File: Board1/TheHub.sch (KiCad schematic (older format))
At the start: 27 parts

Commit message: Add support for RFD900 on USART6
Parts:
- added J?: RFD900, symbol CONN_02X08
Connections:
- net GND: now also J?.1 (P1), J?.16 (P16), J?.2 (P2)
- net PA11: now also J?.7 (P7)
- net PA12: now also J?.9 (P9)
- net 5V renamed +5V
- net +5V: now also J?.4 (P4)
- no-connect marks 19 -> 29
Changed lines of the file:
@@
 NoConn ~ 7650 6750
 NoConn ~ 11150 6750
+$Comp
+L CONN_02X08 J?
+U 1 1 59371070
+P 13700 2900
+F 0 "J?" H 13700 3350 50  0000 C CNN
+F 1 "RFD900" V 13700 2900 50  0000 C CNN
+F 2 "" H 13700 1700 50  0001 C CNN
+F 3 "" H 13700 1700 50  0001 C CNN
+	1    13700 2900
+	1    0    0    -1
+$EndComp
+Text Label 13450 2550 2    60   ~ 0
+GND
+NoConn ~ 13450 2650
+NoConn ~ 13450 2750
+NoConn ~ 13450 3050
+NoConn ~ 13450 3150
+NoConn ~ 13450 3250
+NoConn ~ 13950 3150
+NoConn ~ 13950 3050
+NoConn ~ 13950 2950
+NoConn ~ 13950 2850
+NoConn ~ 13950 2750
+Text Label 13950 2550 0    60   ~ 0
+GND
+Text Label 13950 2650 0    60   ~ 0
+5V
+$Comp
+L +5V #PWR?
+U 1 1 593718A3
+P 14250 2650
+F 0 "#PWR?" H 14250 2500 50  0001 C CNN
+F 1 "+5V" H 14250 2790 50  0000 C CNN
+F 2 "" H 14250 2650 50  0001 C CNN
+F 3 "" H 14250 2650 50  0001 C CNN
+	1    14250 2650
+	1    0    0    -1
+$EndComp
+Wire Wire Line
+	14250 2650 13950 2650
+Wire Wire Line
+	13950 2550 13950 2350
+Wire Wire Line
+	13950 2350 13450 2350
+Wire Wire Line
+	13450 2350 13450 2550
+$Comp
+L GND #PWR?
+U 1 1 59371A35
+P 13750 2350
+F 0 "#PWR?" H 13750 2100 50  0001 C CNN
+F 1 "GND" H 13750 2200 50  0000 C CNN
+F 2 "" H 13750 2350 50  0001 C CNN
+F 3 "" H 13750 2350 50  0001 C CNN
+	1    13750 2350
+	-1   0    0    1
+$EndComp
+Wire Wire Line
+	5450 2550 6050 2550
+Wire Wire Line
+	5450 2450 6050 2450
+Text Label 6050 2550 0    60   ~ 0
+USART6_TX
+Text Label 6050 2450 0    60   ~ 0
+USART6_RX
+Text Label 13450 2850 2    60   ~ 0
+USART6_TX
+Text Label 13450 2950 2    60   ~ 0
+USART6_RX
+$Comp
+L GND #PWR?
+U 1 1 59372AF7
+P 14150 3250
+F 0 "#PWR?" H 14150 3000 50  0001 C CNN
+F 1 "GND" H 14150 3100 50  0000 C CNN
+F 2 "" H 14150 3250 50  0001 C CNN
+F 3 "" H 14150 3250 50  0001 C CNN
+	1    14150 3250
+	0    -1   -1   0
+$EndComp
+Wire Wire Line
+	14150 3250 13950 3250
 $EndSCHEMATC

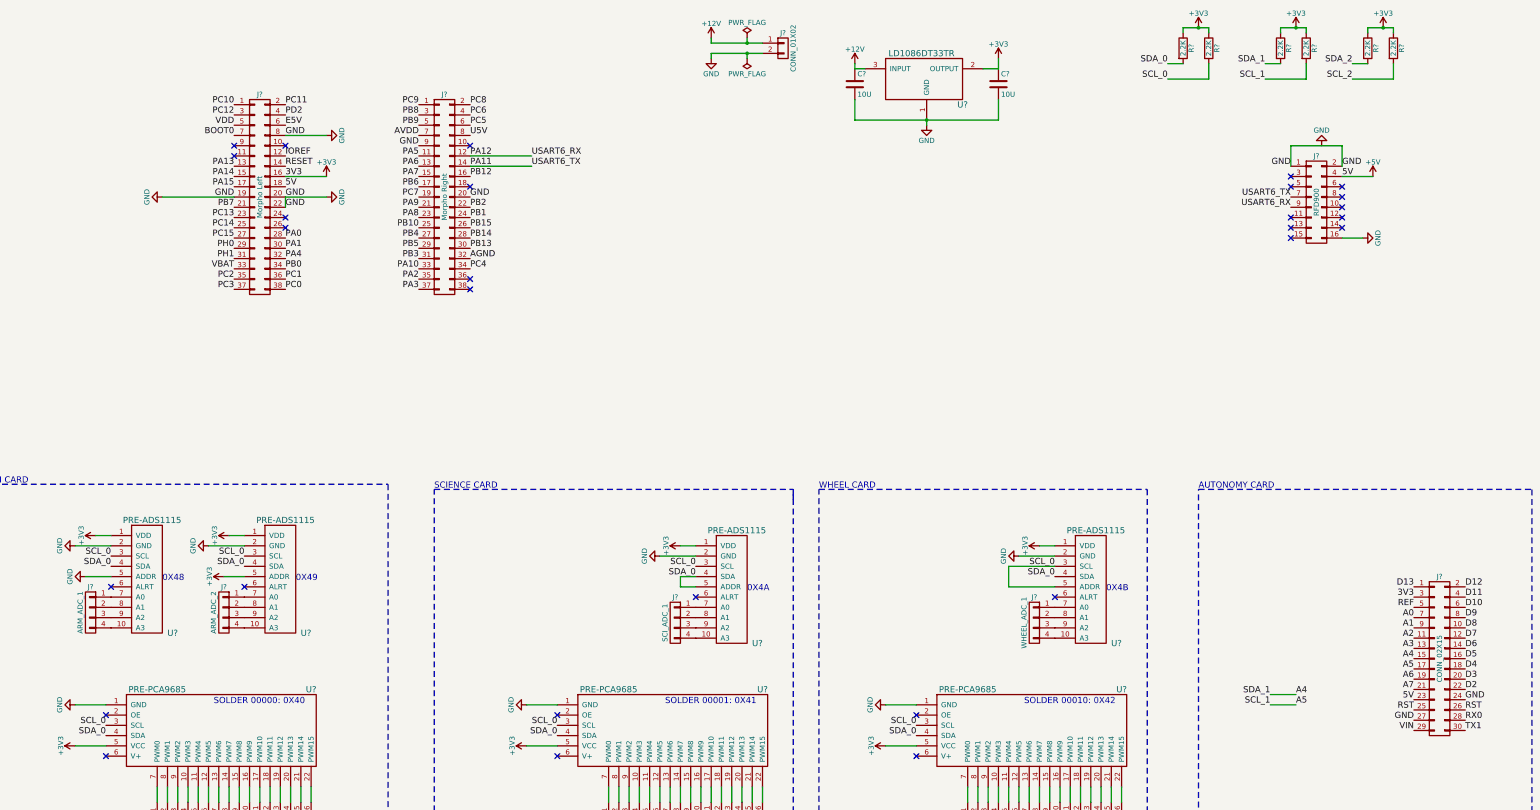
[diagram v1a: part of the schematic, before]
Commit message: Change I2C lines to properly index
I2C starts at 1, not 0
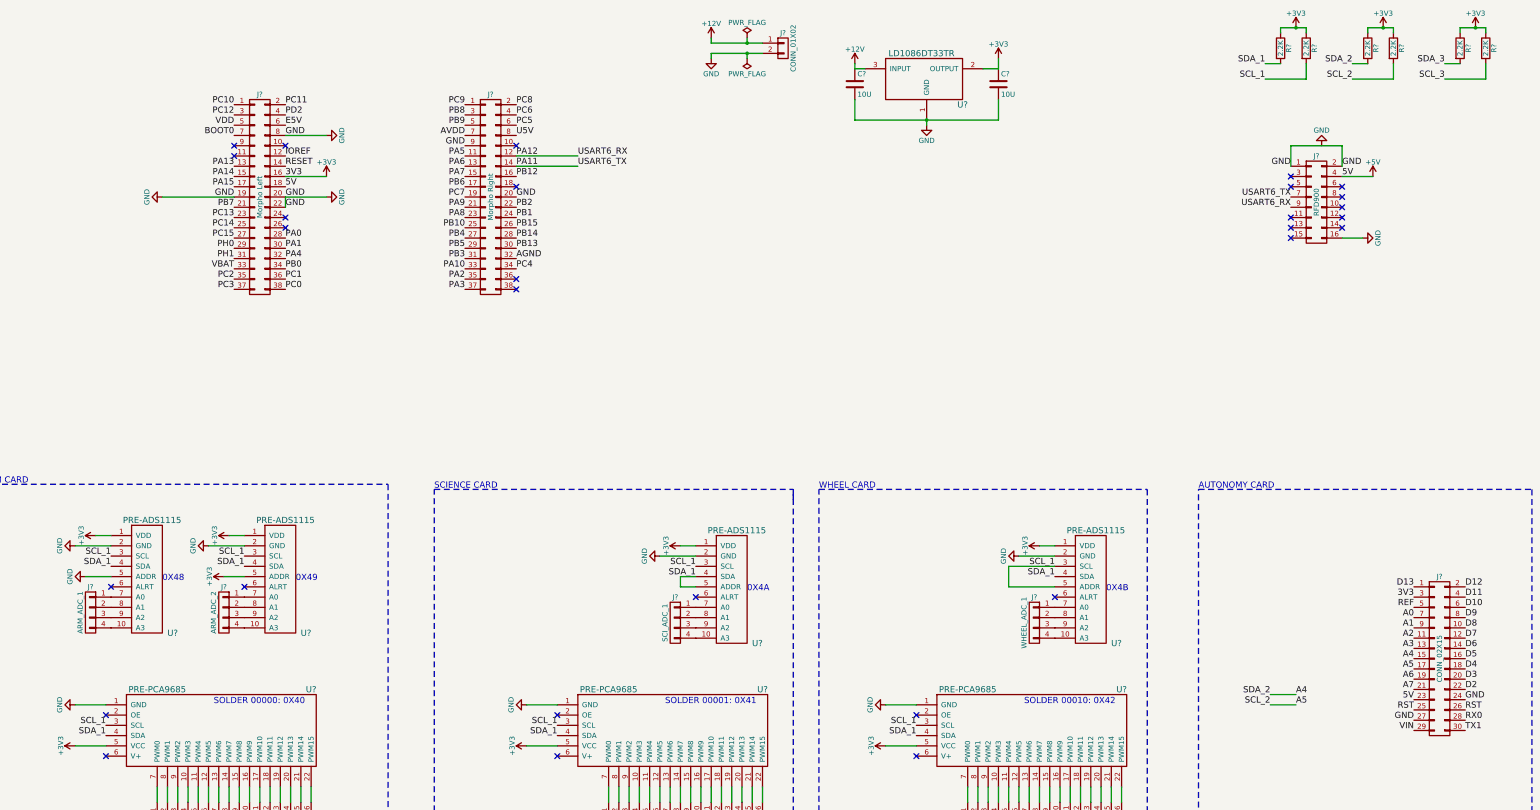
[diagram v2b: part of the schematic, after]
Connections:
- net SCL_2 is gone; now on net A5: R?.2
- net SDA_2 is gone; now on net A4: R?.2
- net A4: no longer R?.2
- net A5: no longer R?.2
- net SCL_0 renamed SCL_1
- net SCL_1: now also R?.2; no longer R?.2
- net SDA_0 renamed SDA_1
- net SDA_1: now also R?.2; no longer R?.2
- new net SCL_3: R?.2
- new net SDA_3: R?.2
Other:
- moved on the sheet: J?, R?
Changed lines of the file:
@@
 L CONN_02X19 J?
 U 1 1 5935F6CD
-P 5200 2850
-F 0 "J?" H 5200 3850 50  0000 C CNN
-F 1 "Morpho Right" V 5200 2850 50  0000 C CNN
-F 2 "" H 5200 1850 50  0001 C CNN
-F 3 "" H 5200 1850 50  0001 C CNN
-	1    5200 2850
+P 5650 2850
+F 0 "J?" H 5650 3850 50  0000 C CNN
+F 1 "Morpho Right" V 5650 2850 50  0000 C CNN
+F 2 "" H 5650 1850 50  0001 C CNN
+F 3 "" H 5650 1850 50  0001 C CNN
+	1    5650 2850
 	1    0    0    -1
 $EndComp
@@
 Text Label 3650 3750 0    60   ~ 0
 PC0
-Text Label 4950 1950 2    60   ~ 0
+Text Label 5400 1950 2    60   ~ 0
 PC9
-Text Label 4950 2050 2    60   ~ 0
+Text Label 5400 2050 2    60   ~ 0
 PB8
-Text Label 4950 2150 2    60   ~ 0
+Text Label 5400 2150 2    60   ~ 0
 PB9
-Text Label 4950 2250 2    60   ~ 0
+Text Label 5400 2250 2    60   ~ 0
 AVDD
-Text Label 4950 2350 2    60   ~ 0
+Text Label 5400 2350 2    60   ~ 0
 GND
-Text Label 4950 2450 2    60   ~ 0
+Text Label 5400 2450 2    60   ~ 0
 PA5
-Text Label 4950 2550 2    60   ~ 0
+Text Label 5400 2550 2    60   ~ 0
 PA6
-Text Label 4950 2650 2    60   ~ 0
+Text Label 5400 2650 2    60   ~ 0
 PA7
-Text Label 4950 2750 2    60   ~ 0
+Text Label 5400 2750 2    60   ~ 0
 PB6
-Text Label 4950 2850 2    60   ~ 0
+Text Label 5400 2850 2    60   ~ 0
 PC7
-Text Label 4950 2950 2    60   ~ 0
+Text Label 5400 2950 2    60   ~ 0
 PA9
-Text Label 4950 3050 2    60   ~ 0
+Text Label 5400 3050 2    60   ~ 0
 PA8
-Text Label 4950 3150 2    60   ~ 0
+Text Label 5400 3150 2    60   ~ 0
 PB10
-Text Label 4950 3250 2    60   ~ 0
+Text Label 5400 3250 2    60   ~ 0
 PB4
-Text Label 4950 3350 2    60   ~ 0
+Text Label 5400 3350 2    60   ~ 0
 PB5
-Text Label 4950 3450 2    60   ~ 0
+Text Label 5400 3450 2    60   ~ 0
 PB3
-Text Label 4950 3550 2    60   ~ 0
+Text Label 5400 3550 2    60   ~ 0
 PA10
-Text Label 4950 3650 2    60   ~ 0
+Text Label 5400 3650 2    60   ~ 0
 PA2
-Text Label 4950 3750 2    60   ~ 0
+Text Label 5400 3750 2    60   ~ 0
 PA3
-Text Label 5450 1950 0    60   ~ 0
+Text Label 5900 1950 0    60   ~ 0
 PC8
-Text Label 5450 2050 0    60   ~ 0
+Text Label 5900 2050 0    60   ~ 0
 PC6
-Text Label 5450 2150 0    60   ~ 0
+Text Label 5900 2150 0    60   ~ 0
 PC5
-Text Label 5450 2250 0    60   ~ 0
+Text Label 5900 2250 0    60   ~ 0
 U5V
-NoConn ~ 5450 2350
-Text Label 5450 2450 0    60   ~ 0
+NoConn ~ 5900 2350
+Text Label 5900 2450 0    60   ~ 0
 PA12
-Text Label 5450 2550 0    60   ~ 0
+Text Label 5900 2550 0    60   ~ 0
 PA11
-Text Label 5450 2650 0    60   ~ 0
+Text Label 5900 2650 0    60   ~ 0
 PB12
-NoConn ~ 5450 2750
-Text Label 5450 2850 0    60   ~ 0
+NoConn ~ 5900 2750
+Text Label 5900 2850 0    60   ~ 0
 GND
-Text Label 5450 2950 0    60   ~ 0
+Text Label 5900 2950 0    60   ~ 0
 PB2
-Text Label 5450 3050 0    60   ~ 0
+Text Label 5900 3050 0    60   ~ 0
 PB1
-Text Label 5450 3150 0    60   ~ 0
+Text Label 5900 3150 0    60   ~ 0
 PB15
-Text Label 5450 3250 0    60   ~ 0
+Text Label 5900 3250 0    60   ~ 0
 PB14
-Text Label 5450 3350 0    60   ~ 0
+Text Label 5900 3350 0    60   ~ 0
 PB13
-Text Label 5450 3450 0    60   ~ 0
+Text Label 5900 3450 0    60   ~ 0
 AGND
-Text Label 5450 3550 0    60   ~ 0
+Text Label 5900 3550 0    60   ~ 0
 PC4
-NoConn ~ 5450 3650
-NoConn ~ 5450 3750
+NoConn ~ 5900 3650
+NoConn ~ 5900 3750
 Text Label 3650 2650 0    60   ~ 0
 3V3
@@
 TX1
 Text Label 13250 7700 2    60   ~ 0
-SDA_1
+SDA_2
 Text Label 13250 7800 2    60   ~ 0
-SCL_1
+SCL_2
 Text Label 13500 7700 0    60   ~ 0
 A4
 Text Label 13500 7800 0    60   ~ 0
 A5
-Text Label 12250 1550 2    60   ~ 0
-SDA_0
-Text Label 12250 1700 2    60   ~ 0
-SCL_0
+Text Label 14950 1550 2    60   ~ 0
+SDA_3
+Text Label 14950 1700 2    60   ~ 0
+SCL_3
 $Comp
 L +3V3 #PWR?
 U 1 1 59364599
-P 12550 1200
-F 0 "#PWR?" H 12550 1050 50  0001 C CNN
-F 1 "+3V3" H 12550 1340 50  0000 C CNN
-F 2 "" H 12550 1200 50  0001 C CNN
-F 3 "" H 12550 1200 50  0001 C CNN
-	1    12550 1200
+P 15250 1200
+F 0 "#PWR?" H 15250 1050 50  0001 C CNN
+F 1 "+3V3" H 15250 1340 50  0000 C CNN
+F 2 "" H 15250 1200 50  0001 C CNN
+F 3 "" H 15250 1200 50  0001 C CNN
+	1    15250 1200
 	1    0    0    -1
 $EndComp
@@
 L R R?
 U 1 1 593645BE
-P 12400 1400
-F 0 "R?" V 12480 1400 50  0000 C CNN
-F 1 "2.2K" V 12400 1400 50  0000 C CNN
-F 2 "" V 12330 1400 50  0001 C CNN
-F 3 "" H 12400 1400 50  0001 C CNN
-	1    12400 1400
+P 15100 1400
+F 0 "R?" V 15180 1400 50  0000 C CNN
+F 1 "2.2K" V 15100 1400 50  0000 C CNN
+F 2 "" V 15030 1400 50  0001 C CNN
+F 3 "" H 15100 1400 50  0001 C CNN
+	1    15100 1400
 	1    0    0    -1
 $EndComp
@@
 L R R?
 U 1 1 593646BD
-P 12650 1400
-F 0 "R?" V 12730 1400 50  0000 C CNN
-F 1 "2.2K" V 12650 1400 50  0000 C CNN
-F 2 "" V 12580 1400 50  0001 C CNN
-F 3 "" H 12650 1400 50  0001 C CNN
-	1    12650 1400
+P 15350 1400
+F 0 "R?" V 15430 1400 50  0000 C CNN
+F 1 "2.2K" V 15350 1400 50  0000 C CNN
+F 2 "" V 15280 1400 50  0001 C CNN
+F 3 "" H 15350 1400 50  0001 C CNN
+	1    15350 1400
 	1    0    0    -1
 $EndComp
@@
 SOLDER 00010: 0X42
 Text Label 1950 6450 2    60   ~ 0
-SDA_0
+SDA_1
 Text Label 1950 6350 2    60   ~ 0
-SCL_0
+SCL_1
 $Comp
 L +3V3 #PWR?
@@
 	13250 7800 13500 7800
 Wire Wire Line
-	12250 1550 12400 1550
-Wire Wire Line
-	12400 1250 12400 1200
-Wire Wire Line
-	12400 1200 12650 1200
-Wire Wire Line
-	12250 1700 12650 1700
-Wire Wire Line
-	12650 1700 12650 1550
-Wire Wire Line
-	12650 1200 12650 1250
-Connection ~ 12550 1200
+	14950 1550 15100 1550
+Wire Wire Line
+	15100 1250 15100 1200
+Wire Wire Line
+	15100 1200 15350 1200
+Wire Wire Line
+	14950 1700 15350 1700
+Wire Wire Line
+	15350 1700 15350 1550
+Wire Wire Line
+	15350 1200 15350 1250
+Connection ~ 15250 1200
 Wire Wire Line
 	13200 1550 13350 1550
@@
 $EndComp
 Text Label 3250 6450 2    60   ~ 0
-SDA_0
+SDA_1
 Text Label 3250 6350 2    60   ~ 0
-SCL_0
+SCL_1
 $Comp
 L +3V3 #PWR?
@@
 $EndComp
 Text Label 7650 6550 2    60   ~ 0
-SDA_0
+SDA_1
 Text Label 7650 6450 2    60   ~ 0
-SCL_0
+SCL_1
 $Comp
 L +3V3 #PWR?
@@
 $EndComp
 Text Label 11150 6550 2    60   ~ 0
-SDA_0
+SDA_1
 Text Label 11150 6450 2    60   ~ 0
-SCL_0
+SCL_1
 $Comp
 L +3V3 #PWR?
@@
 $EndComp
 Text Label 1900 8000 2    60   ~ 0
-SCL_0
+SCL_1
 Text Label 1900 8100 2    60   ~ 0
-SDA_0
+SDA_1
 $Comp
 L GND #PWR?
@@
 $EndComp
 Text Label 6300 8000 2    60   ~ 0
-SCL_0
+SCL_1
 Text Label 6300 8100 2    60   ~ 0
-SDA_0
+SDA_1
 $Comp
 L GND #PWR?
@@
 	6000 8200 6300 8200
 Text Label 9800 8000 2    60   ~ 0
-SCL_0
+SCL_1
 Text Label 9800 8100 2    60   ~ 0
-SDA_0
+SDA_1
 $Comp
 L GND #PWR?
@@
 $EndComp
 Wire Wire Line
-	5450 2550 6050 2550
-Wire Wire Line
-	5450 2450 6050 2450
-Text Label 6050 2550 0    60   ~ 0
+	5900 2550 6500 2550
+Wire Wire Line
+	5900 2450 6500 2450
+Text Label 6500 2550 0    60   ~ 0
 USART6_TX
-Text Label 6050 2450 0    60   ~ 0
+Text Label 6500 2450 0    60   ~ 0
 USART6_RX
 Text Label 13450 2850 2    60   ~ 0

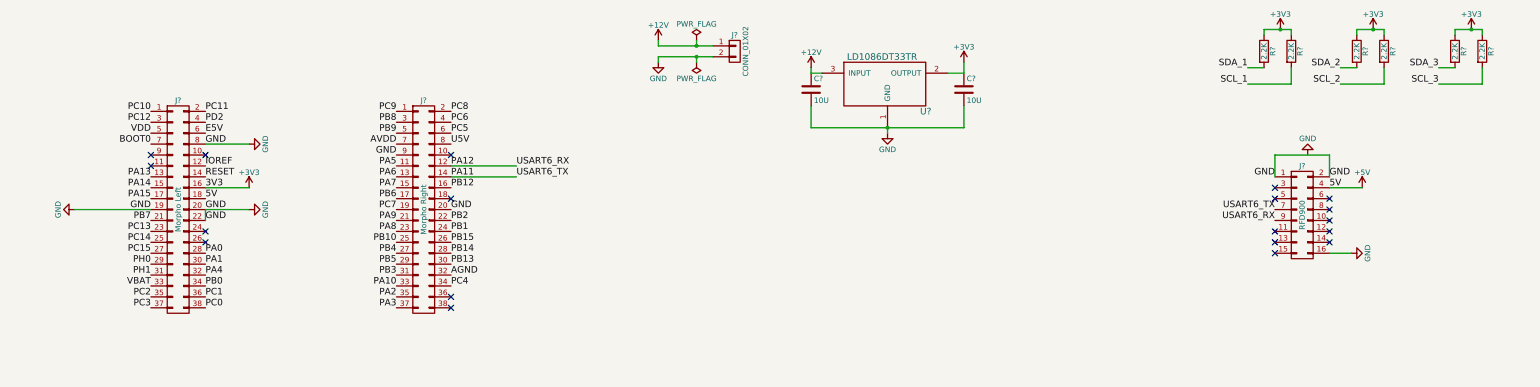
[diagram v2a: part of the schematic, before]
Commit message: Add support for I2C123, add test pins for I2C, add 4 GPIO status LEDs with test pins
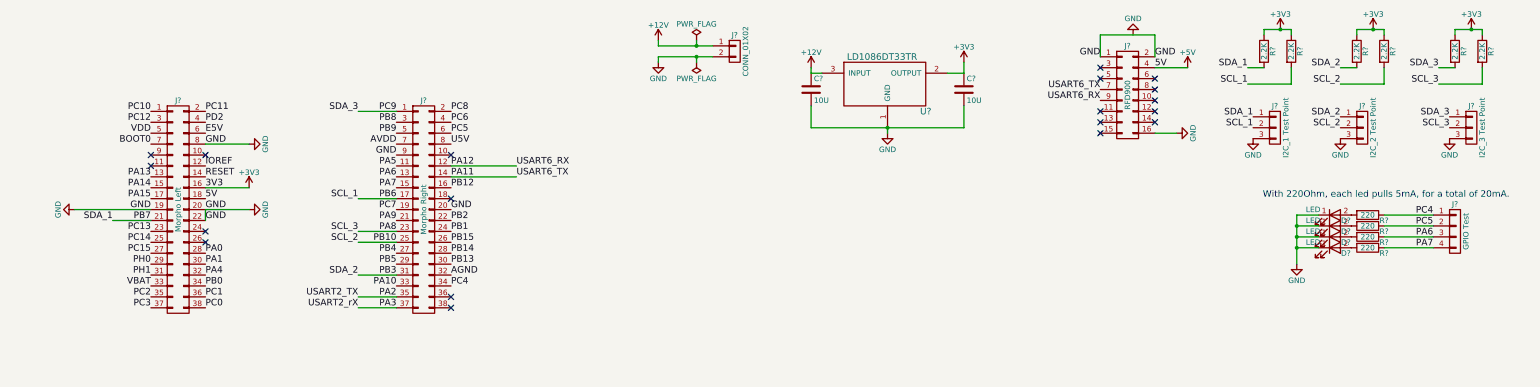
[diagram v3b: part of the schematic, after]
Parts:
- added D? (x4): LED, symbol LED
- added J?: I2C_1 Test Point, symbol CONN_01X03
- added J?: I2C_2 Test Point, symbol CONN_01X03
- added J?: I2C_3 Test Point, symbol CONN_01X03
- added J?: GPIO Test, symbol CONN_01X04
- added R? (x4): 220, symbol R
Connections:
- net PB10 is gone; now on net A5: J?.25 (P25)
- net PB3 is gone; now on net A4: J?.31 (P31)
- net SCL_1 is gone; now on net PB6: R?.2, U?.3 (SCL), U?.3 (SCL), U?.3 (SCL), U?.3 (SCL), U?.3 (SCL), U?.3 (SCL), U?.3 (SCL), U?.5 (ADDR)
- net SCL_3 is gone; now on net PA8: R?.2
- net SDA_1 is gone; now on net PB7: R?.2, U?.4 (SDA), U?.4 (SDA), U?.4 (SDA), U?.4 (SDA), U?.4 (SDA), U?.4 (SDA), U?.4 (SDA), U?.5 (ADDR)
- net SDA_3 is gone; now on net PC9: R?.2
- net A4: now also J?.1 (P1)
- net A5: now also J?.2 (P2)
- net GND: now also D?.1 (K), D?.1 (K), D?.1 (K), D?.1 (K), J?.3 (P3), J?.3 (P3), J?.3 (P3)
- net PA6: now also J?.3 (P3), R?.1
- net PA7: now also J?.4 (P4), R?.1
- net PA8: now also J?.2 (P2)
- net PB6: now also J?.2 (P2)
- net PB7: now also J?.1 (P1)
- net PC4: now also J?.1 (P1), R?.1
- net PC5: now also J?.2 (P2), R?.1
- net PC9: now also J?.1 (P1)
- new net: D?.2 (A), R?.2 (x4)
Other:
- note added: "With 220Ohm, each led pulls 5mA, for a total of 20mA."
- moved on the sheet: J?
